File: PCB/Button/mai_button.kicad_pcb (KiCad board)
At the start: 2 copper layers, 62 x 24 mm, 14 parts, among them J1 Conn_01x03, J2 Conn_01x02, J3 Conn_01x03, J4 Conn_01x02, SW1 SW_DIP_x01

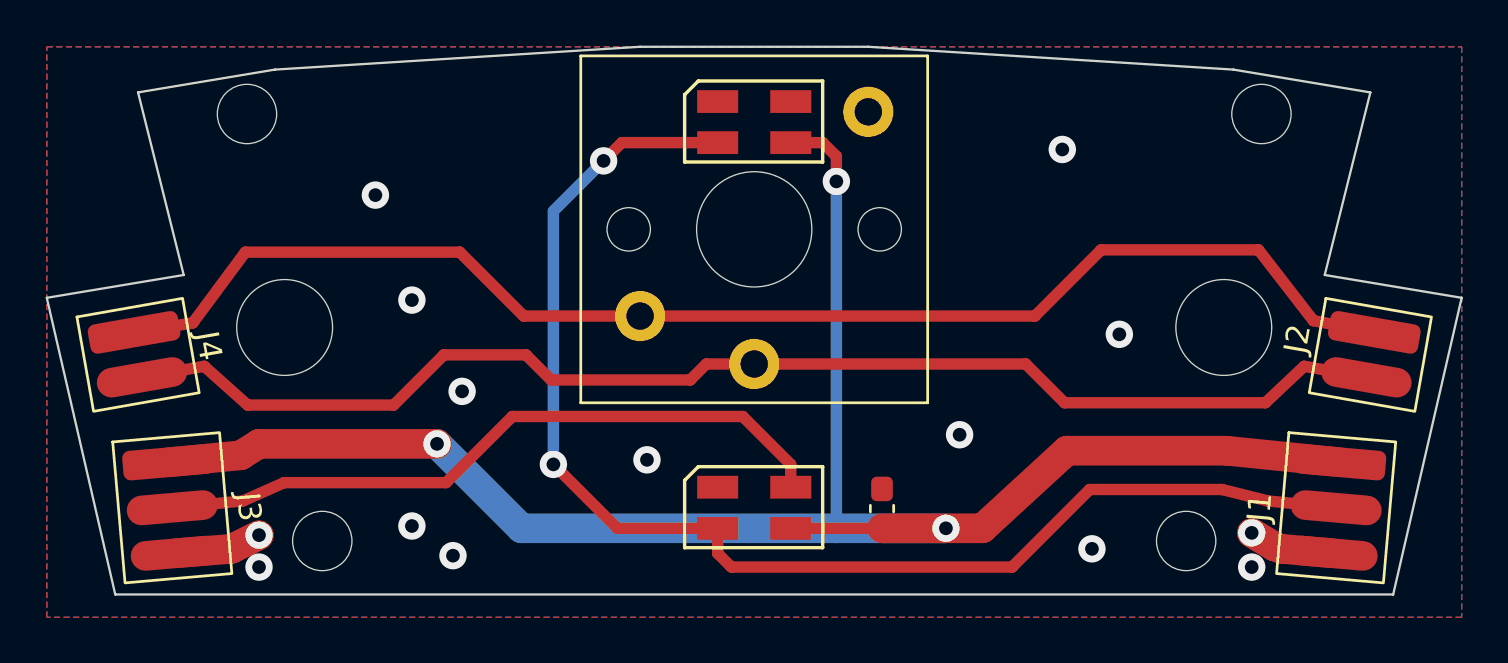
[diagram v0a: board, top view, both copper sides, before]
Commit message: Button PCB update (v1.1)
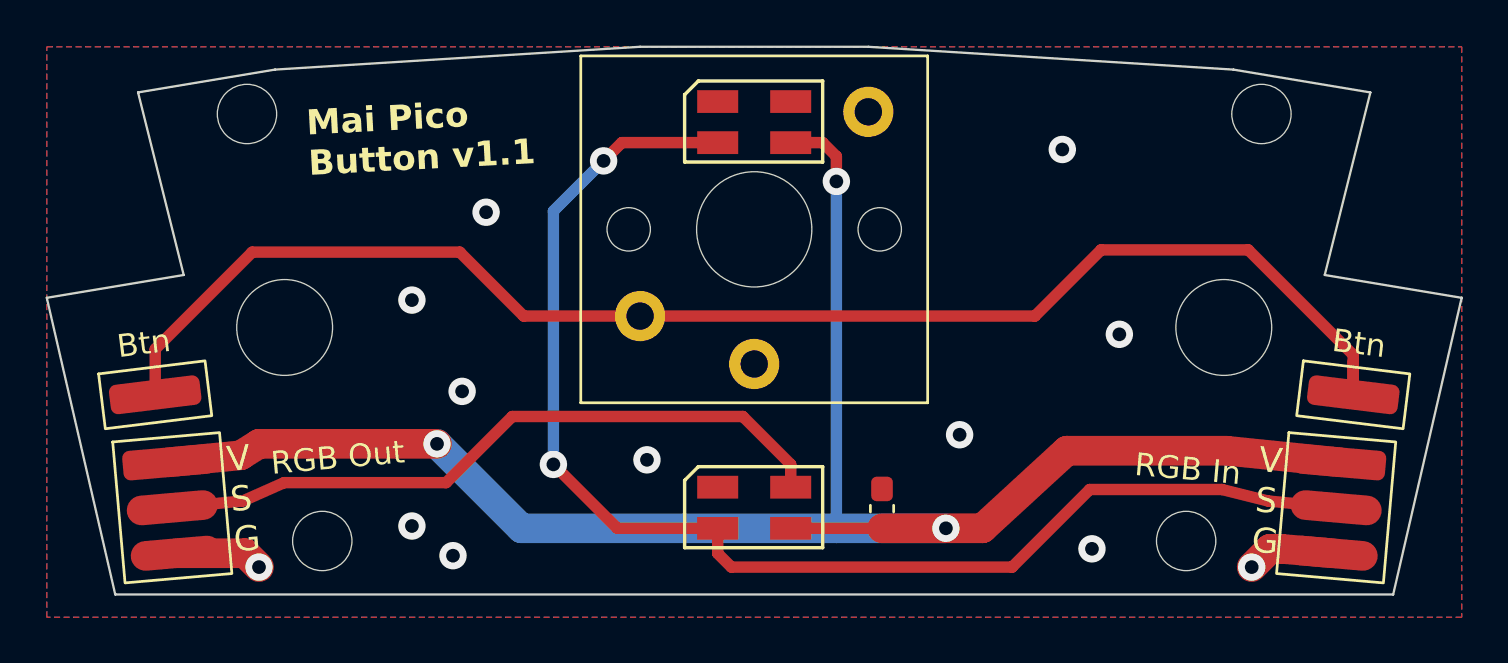
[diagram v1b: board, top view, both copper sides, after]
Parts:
- J1: value Conn_01x03 -> RGB In
- J2, J4: value Conn_01x02 -> Btn; footprint mai_button:Solder_2P -> mai_button:Solder_1P
- J3: value Conn_01x03 -> RGB Out
- moved J2 1.90 mm to (136.6, 139.7), turned to -7 degrees
- moved J4 1.90 mm to (84.1, 139.7), turned to 7 degrees
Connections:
- SW1 pad 1: Net-(J4-Pad2) -> GND
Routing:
- net Net-(J4-Pad2): track 57.4 -> 0.00 mm
- net Net-(J2-Pin_1): track 59.9 -> 63.8 mm
- net GND: track 7.49 -> 7.74 mm, vias 14 -> 12
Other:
- board text added: "Mai Pico Button v1.1"
- board text added: "V S G"
